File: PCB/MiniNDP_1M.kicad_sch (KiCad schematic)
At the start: 19 parts, among them J1 Conn_02x20_Odd_Even, U1 HC161, U2 HC161, U3 HC161, U4 HC138, U5 FCT821, U6 AS6C8008_TSOPII, U7 1G32

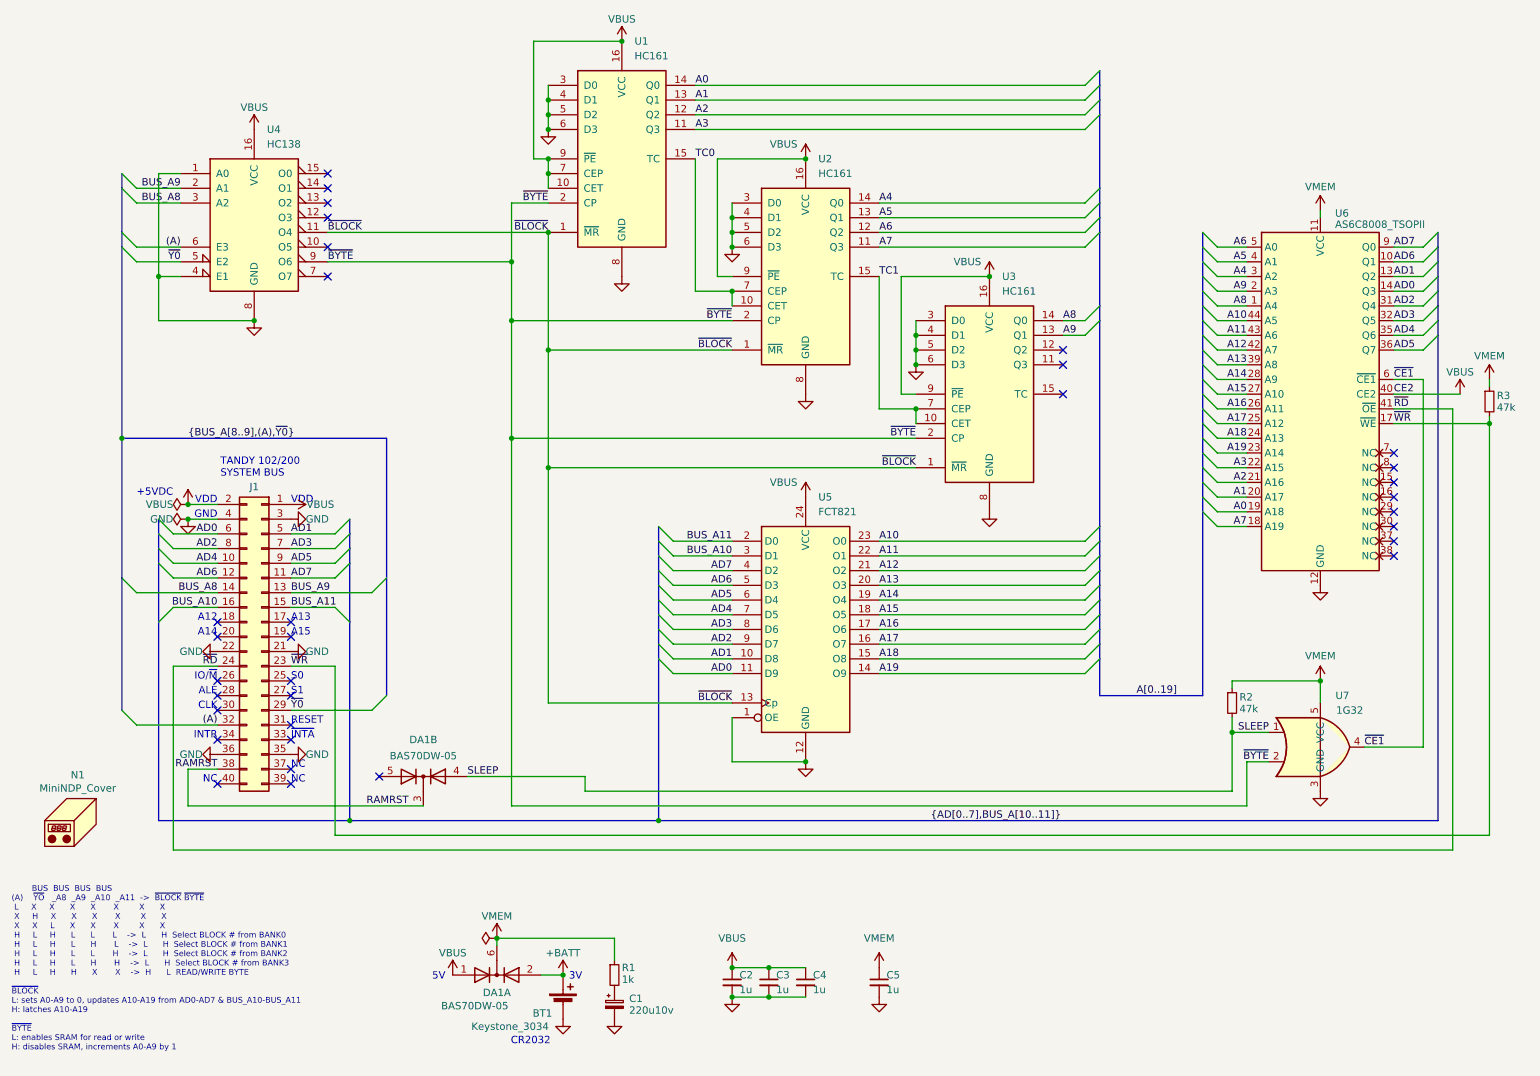
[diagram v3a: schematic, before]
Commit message: 1M_C 1 meg based on 4040
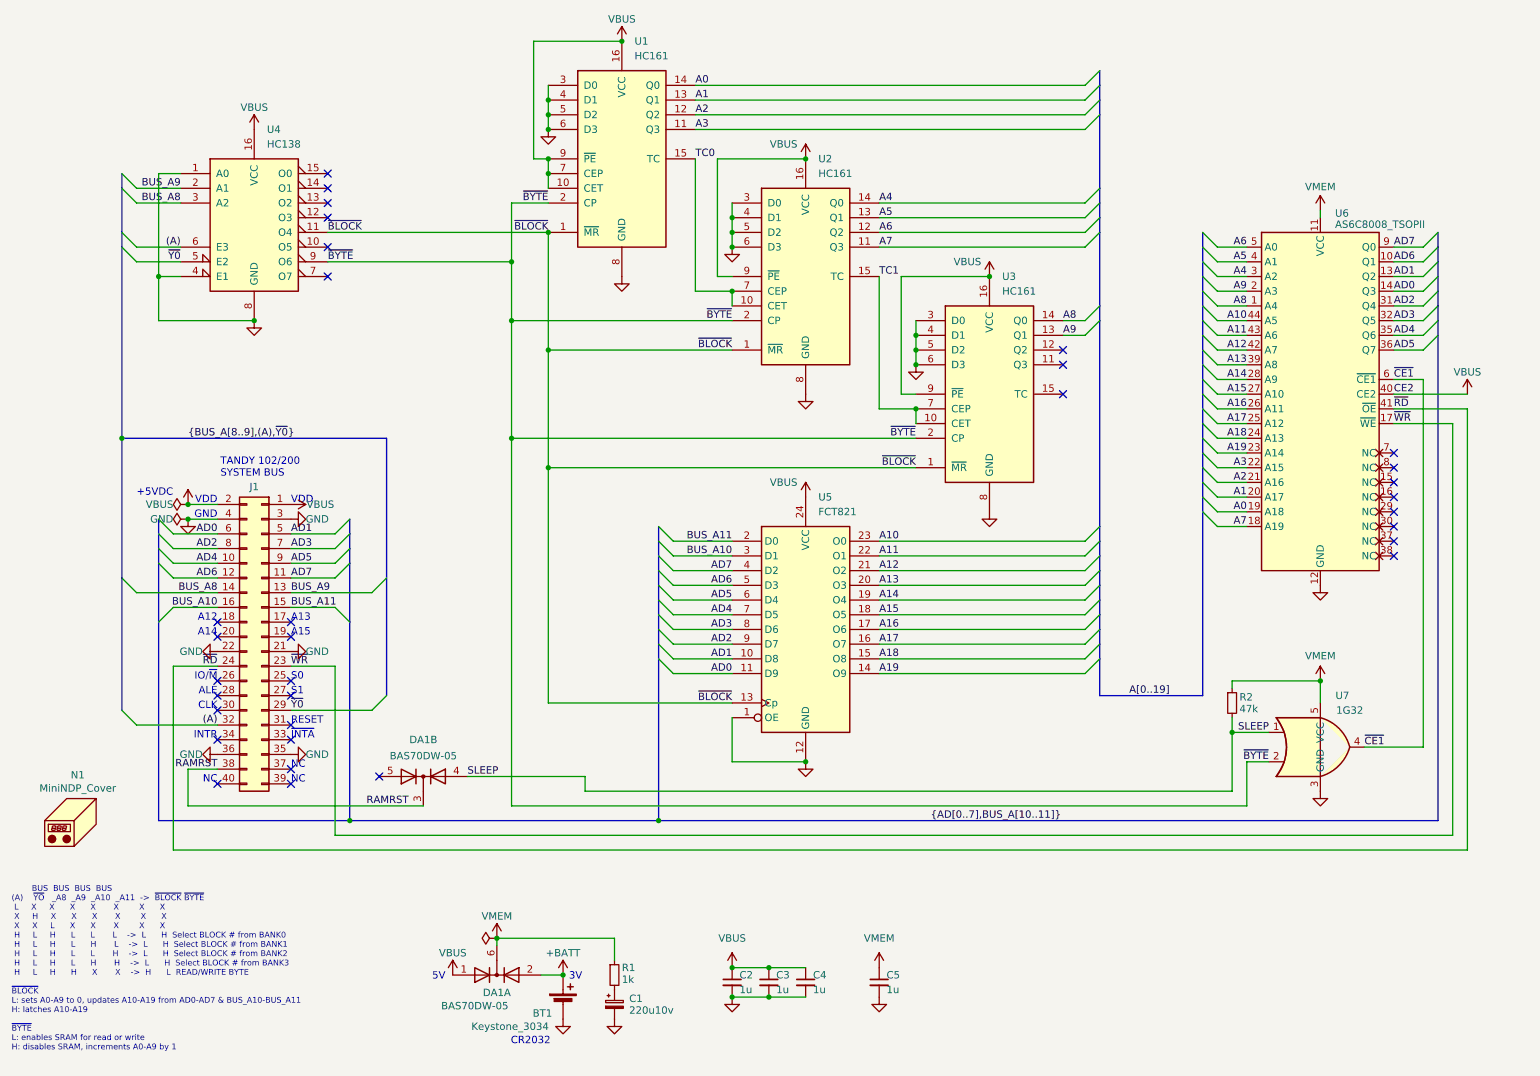
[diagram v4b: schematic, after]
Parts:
- removed R3: 47k, 000_LOCAL:R_0805, symbol 000_LOCAL:R
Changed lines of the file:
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@@
 	(title_block
 		(title "MiniNDP 1M")
-		(date "2024-11-13")
-		(rev "B03")
+		(date "2024-11-26")
+		(rev "B04")
 		(company "Brian K. White - b.kenyon.w@gmail.com")
 		(comment 1 "github.com/bkw777/NODE_DATAPAC")
@@
 	)
 	(junction
-		(at 270.51 86.36)
-		(diameter 0)
-		(color 0 0 0 0)
-	)
-	(junction
 		(at 139.7 63.5)
 		(diameter 0)
@@
 	(wire
 		(pts
-			(xy 270.51 85.09) (xy 270.51 86.36)
-		)
-		(stroke
-			(width 0)
-			(type default)
-		)
-	)
-	(wire
-		(pts
 			(xy 223.52 93.98) (xy 228.6 93.98)
 		)
@@
 	(wire
 		(pts
-			(xy 270.51 86.36) (xy 270.51 157.48)
+			(xy 264.16 86.36) (xy 264.16 157.48)
 		)
 		(stroke
@@
 	(wire
 		(pts
-			(xy 270.51 78.74) (xy 270.51 80.01)
-		)
-		(stroke
-			(width 0)
-			(type default)
-		)
-	)
-	(wire
-		(pts
 			(xy 101.6 68.58) (xy 101.6 88.9)
 		)
@@
 	(wire
 		(pts
-			(xy 254 86.36) (xy 270.51 86.36)
+			(xy 254 86.36) (xy 264.16 86.36)
 		)
 		(stroke
@@
 	(wire
 		(pts
-			(xy 265.43 81.28) (xy 254 81.28)
+			(xy 266.7 81.28) (xy 254 81.28)
 		)
 		(stroke
@@
 	(wire
 		(pts
-			(xy 270.51 157.48) (xy 71.12 157.48)
+			(xy 264.16 157.48) (xy 71.12 157.48)
 		)
 		(stroke
@@
 	(wire
 		(pts
-			(xy 254 83.82) (xy 264.16 83.82)
+			(xy 254 83.82) (xy 266.7 83.82)
 		)
 		(stroke
@@
 	(wire
 		(pts
-			(xy 264.16 160.02) (xy 264.16 83.82)
+			(xy 266.7 160.02) (xy 266.7 83.82)
 		)
 		(stroke
@@
 	(wire
 		(pts
-			(xy 43.18 160.02) (xy 264.16 160.02)
+			(xy 43.18 160.02) (xy 266.7 160.02)
 		)
 		(stroke
@@
 	)
 	(label "A[0..19]"
-		(at 209.55 133.35 0)
+		(at 208.28 133.35 0)
 		(fields_autoplaced yes)
 		(effects
@@
 	(symbol
 		(lib_id "power:VBUS")
-		(at 265.43 81.28 0)
+		(at 266.7 81.28 0)
 		(unit 1)
 		(exclude_from_sim no)
@@
 		(dnp no)
 		(property "Reference" "#PWR026"
-			(at 265.43 85.09 0)
+			(at 266.7 85.09 0)
 			(effects
 				(font
@@
 		)
 		(property "Value" "VBUS"
-			(at 265.43 77.47 0)
+			(at 266.7 77.47 0)
 			(effects
 				(font
@@
 		)
 		(property "Footprint" ""
-			(at 265.43 81.28 0)
+			(at 266.7 81.28 0)
 			(effects
 				(font
@@
 		)
 		(property "Datasheet" ""
-			(at 265.43 81.28 0)
+			(at 266.7 81.28 0)
 			(effects
 				(font
@@
 		)
 		(property "Description" "Power symbol creates a global label with name \"VBUS\""
-			(at 265.43 81.28 0)
+			(at 266.7 81.28 0)
 			(effects
 				(font
@@
 	)
 	(symbol
-		(lib_id "power:VMEM")
-		(at 270.51 78.74 0)
-		(unit 1)
-		(exclude_from_sim no)
-		(in_bom yes)
-		(on_board yes)
-		(dnp no)
-		(property "Reference" "#PWR013"
-			(at 270.51 82.55 0)
-			(effects
-				(font
-					(size 1.27 1.27)
-				)
-				(hide yes)
-			)
-		)
-		(property "Value" "VMEM"
-			(at 270.51 74.676 0)
-			(effects
-				(font
-					(size 1.27 1.27)
-				)
-			)
-		)
-		(property "Footprint" ""
-			(at 270.51 78.74 0)
-			(effects
-				(font
-					(size 1.27 1.27)
-				)
-				(hide yes)
-			)
-		)
-		(property "Datasheet" ""
-			(at 270.51 78.74 0)
-			(effects
-				(font
-					(size 1.27 1.27)
-				)
-				(hide yes)
-			)
-		)
-		(property "Description" "Power symbol creates a global label with name \"VMEM\""
-			(at 270.51 78.74 0)
-			(effects
-				(font
-					(size 1.27 1.27)
-				)
-				(hide yes)
-			)
-		)
-		(pin "1"
-		)
-		(instances
-			(project "MiniNDP_1M"
-				(path "/f15c2929-5cf4-4b4e-965d-148e1bec8a42"
-					(reference "#PWR013")
-					(unit 1)
-				)
-			)
-		)
-	)
-	(symbol
 		(lib_id "power:GND")
 		(at 139.7 55.88 0)
@@
 					(unit 1)
 				)
-			)
-		)
-	)
-	(symbol
-		(lib_id "000_LOCAL:R")
-		(at 270.51 82.55 0)
-		(unit 1)
-		(exclude_from_sim no)
-		(in_bom yes)
-		(on_board yes)
-		(dnp no)
-		(property "Reference" "R3"
-			(at 271.78 81.534 0)
-			(effects
-				(font
-					(size 1.27 1.27)
-				)
-				(justify left)
-			)
-		)
-		(property "Value" "47k"
-			(at 271.78 83.566 0)
-			(effects
-				(font
-					(size 1.27 1.27)
-				)
-				(justify left)
-			)
-		)
-		(property "Footprint" "000_LOCAL:R_0805"
-			(at 270.51 82.55 0)
-			(effects
-				(font
-					(size 1.27 1.27)
-				)
-				(hide yes)
-			)
-		)
-		(property "Datasheet" "datasheets/sei-rmcf_rmcp.pdf"
-			(at 270.51 82.55 0)
-			(effects
-				(font
-					(size 1.27 1.27)
-				)
-				(hide yes)
-			)
-		)
-		(property "Description" "RES 47K OHM 1% 1/8W 0805"
-			(at 270.51 82.55 0)
-			(effects
-				(font
-					(size 1.27 1.27)
-				)
-				(hide yes)
-			)
-		)
-		(property "MPN" "RMCF0805FT47K0"
-			(at 270.51 82.55 0)
-			(effects
-				(font
-					(size 1.27 1.27)
-				)
-				(hide yes)
-			)
-		)
-		(pin "1"
-		)
-		(pin "2"
-		)
-		(instances
-			(project "MiniNDP_1M"
-				(path "/f15c2929-5cf4-4b4e-965d-148e1bec8a42"
-					(reference "R3")
-					(unit 1)
-				)
